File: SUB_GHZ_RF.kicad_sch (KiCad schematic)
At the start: 231 parts, among them J3 SMA4, J4 SMA1_CH-A_50R, J5 SMA2_CH-B_50R, J6 SMA3_CH-C_50R, T1 B0310J50100AHF, T2 B0310J50100AHF, T3 B0310J50100AHF, U10 BGS12WN6E6327XTSA1, U12 BGS12WN6E6327XTSA1, U14 TQP3M9036, U15 TSS-13LN+, U16 TCA9535PWR, U17 TQP3M9036, U18 BGS13SN8, U19 BGS13SN8, U20 BGS13SN8E6327XTSA1, U21 BGS13SN8E6327XTSA1, U22 TQP7M9106, U27 TPS22918DBVR, U28 BGS12P2L6, U29 BGS12P2L6, U3 CC1101RGPR, U30 BGS12P2L6, U31 BGS12P2L6, U4 CC1101RGPR, U5 CC1101RGPR, U6 SI4463-C2A-GM, U7 BGS12WN6E6327XTSA1, U8 BGS13SN8E6327XTSA1, U9 BGS13SN8E6327XTSA1, Y1 Epson X1E0000210143, Y2 Epson X1E0000210143, Y3 Epson X1E0000210143, Y4 NX2016SA

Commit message: Finished Last sheets
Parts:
- R59, R62: value 33k -> 10k
- R60, R61: value 10k -> 33k
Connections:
- net GND: no longer U6.5 (NC)
- no-connect marks 8 -> 9
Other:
- moved on the sheet: C42

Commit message: finished annotation
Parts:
- removed R44, R45: 10k, symbol Device:R
- added D15: RClamp2451ZA, Diode_SMD:Nexperia_DSN0603-2_0.6x0.3mm_P0.4mm, symbol Device:D_TVS
- added R141, R58, R59: 10k, symbol Device:R
- C60: renamed from C135; value 60u -> 68u
- D1: footprint (none) -> Diode_SMD:Nexperia_DSN0603-2_0.6x0.3mm_P0.4mm
- D2: value RF_ESD_SMA2_TBD -> RCLAMP2451ZA
- D3: value RF_ESD_SMA3_TBD -> PESD5V0Z1BDSF
- J3, J5, J6: footprint (none) -> Connector_Coaxial:SMA_Amphenol_132289_EdgeMount
- L22: value 18n -> TUNE
- R60: renamed from R62; value 10k -> 0R
- R61: value 33k -> 10k
- U14, U17: footprint TQP3M9036:SON50P200X200X95-9N -> TQP3M:SON50P200X200X95-9N
- U18, U19: value BGS13SN8 -> BGS13SN8E6327XTSA1
- U3, U4, U5: footprint CC1101RGPR:QFN50P400X400X100-21N -> CC1101:QFN50P400X400X100-21N
- Y1, Y2, Y3: footprint (none) -> Crystal:Crystal_SMD_3225-4Pin_3.2x2.5mm
- Y4: value NX2016SA -> NX2016SA-30.000MHz-EXS00A-CS06568
- renumbered C122 to C100, C123 to C101, C124 to C102, C48 to C103, C43 to C104, C44 to C105, C45 to C106, C46 to C107, C47 to C108, C89 to C109, C90 to C110, C49 to C111, C50 to C112, C87 to C113, C86 to C114, C88 to C115, C51 to C116, C52 to C117, C42 to C118, C94 to C119, C99 to C120, C93 to C121, C95 to C122, C97 to C123, C98 to C124, C96 to C125, C66 to C126, C67 to C127, C68 to C128, C70 to C129, C72 to C130, C73 to C131, C69 to C132, C71 to C134, C64 to C135, C65 to C136, C74 to C137, C112 to C138, C113 to C139, C114 to C140, C100 to C141, C101 to C142, C103 to C143, C102 to C144, C115 to C145, C116 to C146, C117 to C147, C104 to C148, C41 to C149, C78 to C42, C84 to C43, C85 to C44, C75 to C45, C76 to C46, C77 to C47, C80 to C48, C79 to C49, C81 to C50, C82 to C51, C83 to C52, C128 to C53, C127 to C54, C126 to C55, C125 to C56, C136 to C57, C138 to C58, C137 to C59, C134 to C61, C133 to C62, C132 to C63, C131 to C64, C129 to C65, C130 to C66, C139 to C67, C140 to C68, C141 to C69, C142 to C70, C143 to C71, C144 to C72, C145 to C73, C146 to C74, C147 to C75, C109 to C76, C110 to C77, C111 to C78, C58 to C79, C60 to C80, C54 to C81, C55 to C82, C63 to C83, C53 to C84, C56 to C85, C57 to C86, C59 to C87, C61 to C88, C62 to C89, C105 to C90, C106 to C91, C107 to C92, C108 to C93, C91 to C94, C92 to C95, C120 to C96, C119 to C97, C118 to C98, C121 to C99, R58 to R139, R56 to R32, R54 to R33, R55 to R34, R65 to R35, R64 to R36, R57 to R37, R47 to R38, R49 to R39, R48 to R40, R60 to R41, R59 to R42, R75 to R43, R71 to R44, R70 to R45, R67 to R46, R66 to R47, R74 to R48, R72 to R49, R73 to R50, R69 to R51, R68 to R52, R52 to R53, R50 to R54, R76 to R55, R53 to R56, R51 to R57, R63 to R62, R37 to R63, R38 to R64, R36 to R65, R34 to R66, R35 to R67, R32 to R68, R31 to R69, R46 to R70, R42 to R71, R41 to R72, R40 to R73, R39 to R74
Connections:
- net +3V3: now also R61.1; no longer FB6.1
- net +5V_SYS: now also FB6.1
- net CC1101_A_SMA1_PORT: now also D15.2 (A2)
- net GND: now also D15.1 (A1), R58.2, R59.2; no longer R61.1
- net RFX_SAW_C_SEL0: now also R58.1
- net RFX_SAW_C_SEL1: now also R59.1
- net SI4463_SDN: now also R141.2
- net VCC_SI4463: now also R141.1
- net SI4463_nIRQ renamed SI4463_IRQ_N
- no-connect marks 9 -> 11
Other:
- note added: "CHANNEL B — CC1101 + PA2 + SMA2"
- note added: "Firmware Notes CHANNEL-A SAFE DEFAULT: SEL1=0, SEL0=0, RF_SW_A=0, LNA_SD_A=1, PA_SD_A=1. TX SEQUENCE: Disable LNA → select band → select TX path → enable PA → start CC1101 transmission. TX STOP: Stop CC1101 → disable PA → wait ≥10 us → select RX path → enable LNA. GDO0/REPLAY_OUT: Never drive REPLAY_OUT while CC1101 GDO0 is configured as a push-pull output."
- note added: "Firmware note: SAFE DEFAULT: SEL1=0, SEL0=0, PA_EN_B=0. SELECT BAND BEFORE ENABLING PA. DISABLE PA BEFORE CHANGING BAND."
- note added: "PA INPUT/OUTPUT MATCHING AND 315/433/868 MHz LPF VALUES REQUIRE RF SIMULATION AND VNA TUNING BEFORE PRODUCTION"
- note added: "SHARED SUB-GHz CONTROL, SAFE STARTUP & RF RAIL FILTERING"
- note added: "SMA4 / SI4463 REV-A RF MATCHING: 868 MHz ONLY"
- note removed: ". CHANNEL B — CC1101 + PA2 + SMA2"
- note removed: "SHARED RF CONTROL"
- note removed: "SMA1 ESD DEVICE TBD AFTER PA1 POUT/VSWR IS FROZEN"
- note removed: "U7 + J3 — ANTENNA SWITCH AND SMA4"
- title: (none) -> Sub-GHz RF Transceivers, Front Ends and Band-Selectable
- moved on the sheet: R61

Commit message: finished ANCHOR_DOCK sheet
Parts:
- removed C60: 68u, symbol Device:C
- removed R52: TUNE, symbol Device:R
- added C60: 68u, symbol Device:C_Polarized
- added J17: SMA5_RESERVED_CC1200, Connector_Coaxial:SMA_Amphenol_132289_EdgeMount, symbol Connector:Conn_Coaxial
- added J18: SMA6_RESERVED_DUAL_RF, Connector_Coaxial:SMA_Amphenol_132289_EdgeMount, symbol Connector:Conn_Coaxial
- added L36: 4n7, Inductor_SMD:L_0402_1005Metric, symbol Device:L
- C100, C97: footprint (none) -> Capacitor_SMD:C_0603_1608Metric; DISTRIBUTOR_LINK (none) -> https://www.mouser.com/ProductDetail/Murata-Electronics/GRM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; MANUFACTURER (none) -> Murata; MPN (none) -> GRM188R71A225KE15D; Notes (none) -> N/A
- C101, C61, C63: footprint (none) -> Capacitor_SMD:C_0402_1005Metric; DISTRIBUTOR_LINK (none) -> https://www.mouser.com/ProductDetail/Murata-Electronics/GRM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; MANUFACTURER (none) -> Murata; MPN (none) -> GRM1555C1H102JA01D; Notes (none) -> N/A
- C102: footprint (none) -> Capacitor_SMD:C_0805_2012Metric; DISTRIBUTOR_LINK (none) -> https://www.mouser.com/ProductDetail/Murata-Electronics/GRM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; MANUFACTURER (none) -> Murata; MPN (none) -> GRM21BR71A106KE51L; Notes (none) -> Verify effective capacitance under DC bias.
- C103, C104, C105, C106, C107, C108, C112, C118, C119, C121, C126, C127, C128, C129, C130, C131, C134, C137, C147, C148, C149, C42, C46, C47, C80, C83, C84, C85, C86, C87, C88, C89, C90, C93, C94, C95, C98, C99: footprint (none) -> Capacitor_SMD:C_0402_1005Metric; DISTRIBUTOR_LINK (none) -> https://www.mouser.com/ProductDetail/Murata-Electronics/GRM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; MANUFACTURER (none) -> Murata; MPN (none) -> GRM155R71C104KA88D; Notes (none) -> N/A
- C109, C145, C91: footprint (none) -> Capacitor_SMD:C_0402_1005Metric; DISTRIBUTOR_LINK (none) -> N/A; MANUFACTURER (none) -> DNP; MPN (none) -> N/A; Notes (none) -> DNP; tuning pads retained.
- C110, C146, C92: footprint (none) -> Capacitor_SMD:C_0402_1005Metric; DISTRIBUTOR_LINK (none) -> https://www.mouser.com/ProductDetail/Murata-Electronics/GJM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; MANUFACTURER (none) -> Murata; MPN (none) -> GJM1555C1H1R2BB01D; Notes (none) -> N/A
- C111, C124, C132, C143, C45, C58, C79: footprint (none) -> Capacitor_SMD:C_0603_1608Metric; DISTRIBUTOR_LINK (none) -> https://www.mouser.com/ProductDetail/Murata-Electronics/GRM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; MANUFACTURER (none) -> Murata; MPN (none) -> GRM188R71C105KA12D; Notes (none) -> N/A
- C113, C115, C120, C122, C123, C125, C138, C139, C141, C142, C144, C53, C57, C59, C62, C76, C77: footprint (none) -> Capacitor_SMD:C_0402_1005Metric; DISTRIBUTOR_LINK (none) -> https://eu.mouser.com/en/ProductDetail/Murata-Electronics/G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; MANUFACTURER (none) -> Murata; MPN (none) -> GRM1555C1H101JA01D
- C114, C140, C78: footprint (none) -> Capacitor_SMD:C_0402_1005Metric; DISTRIBUTOR_LINK (none) -> https://www.mouser.com/ProductDetail/Murata-Electronics/GJM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; MANUFACTURER (none) -> Murata; MPN (none) -> GJM1555C1HR60BB01D; Notes (none) -> N/A
- C116, C117, C135, C136, C81, C82: footprint (none) -> Capacitor_SMD:C_0402_1005Metric; DISTRIBUTOR_LINK (none) -> https://www.mouser.com/ProductDetail/Murata-Electronics/GJM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; MANUFACTURER (none) -> Murata; MPN (none) -> GJM1555C1H150JB01D; Notes (none) -> N/A
- C43, C44: footprint (none) -> Capacitor_SMD:C_0402_1005Metric; DISTRIBUTOR_LINK (none) -> https://www.mouser.com/ProductDetail/Murata-Electronics/GJM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; MANUFACTURER (none) -> Murata; MPN (none) -> GJM1555C1H4R7BB01D; Notes (none) -> N/A
- C48: footprint (none) -> Capacitor_SMD:C_0402_1005Metric; DISTRIBUTOR_LINK (none) -> https://www.mouser.com/ProductDetail/Murata-Electronics/GJM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; MANUFACTURER (none) -> Murata; MPN (none) -> GJM1555C1H1R0BB01D; Notes (none) -> N/A
- C49: footprint (none) -> Capacitor_SMD:C_0402_1005Metric; DISTRIBUTOR_LINK (none) -> https://www.mouser.com/ProductDetail/Murata-Electronics/GJM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; MANUFACTURER (none) -> Murata; MPN (none) -> GJM1555C1H3R0BB01D; Notes (none) -> N/A
- C50: footprint (none) -> Capacitor_SMD:C_0402_1005Metric; DISTRIBUTOR_LINK (none) -> https://www.mouser.com/ProductDetail/Murata-Electronics/GJM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; MANUFACTURER (none) -> Murata; MPN (none) -> GJM1555C1H3R9BB01D; Notes (none) -> N/A
- C51: footprint (none) -> Capacitor_SMD:C_0402_1005Metric; DISTRIBUTOR_LINK (none) -> https://www.mouser.com/ProductDetail/Murata-Electronics/GJM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; MANUFACTURER (none) -> Murata; MPN (none) -> GJM1555C1H5R1BB01D; Notes (none) -> N/A
- C52: footprint (none) -> Capacitor_SMD:C_0402_1005Metric; DISTRIBUTOR_LINK (none) -> https://www.mouser.com/ProductDetail/Murata-Electronics/GJM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; MANUFACTURER (none) -> Murata; MPN (none) -> GJM1555C1H2R7BB01D; Notes (none) -> N/A
- C54: value TUNE -> 100p; footprint (none) -> Capacitor_SMD:C_0402_1005Metric; DISTRIBUTOR_LINK (none) -> https://eu.mouser.com/en/ProductDetail/Murata-Electronics/G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; MANUFACTURER (none) -> Murata; MPN (none) -> GRM1555C1H101JA01D; Notes (none) -> C0G; initial PA input match; tune on Rev-A.; TUNING_ALTERNATIVES (none) -> ALT-HB:22p; KIT:47p,68p
- C55: value TUNE -> 8p2; footprint (none) -> Capacitor_SMD:C_0402_1005Metric; DISTRIBUTOR_LINK (none) -> https://www.mouser.com/ProductDetail/Murata-Electronics/GJM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; MANUFACTURER (none) -> Murata; MPN (none) -> GJM1555C1H8R2DB01D; Notes (none) -> Initial PA input match; tuning alternatives: DNP, 5.6pF.; TUNING_ALTERNATIVES (none) -> ALT-HB:DNP; KIT:5.6p,6.8p
- C56: value TUNE -> 15p; footprint (none) -> Capacitor_SMD:C_0402_1005Metric; DISTRIBUTOR_LINK (none) -> https://www.mouser.com/ProductDetail/Murata-Electronics/GJM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; MANUFACTURER (none) -> Murata; MPN (none) -> GJM1555C1H150JB01D; Notes (none) -> Initial PA input match; tuning alternative: DNP.; TUNING_ALTERNATIVES (none) -> ALT-HB:5.6p; KIT:8.2p,12p
- C64: value 100p -> 22p; footprint (none) -> Capacitor_SMD:C_0402_1005Metric; DISTRIBUTOR_LINK (none) -> https://eu.mouser.com/en/ProductDetail/Murata-Electronics/G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; MANUFACTURER (none) -> Murata; MPN (none) -> GJM1555C1H220JB01D; Notes (none) -> N/A; TUNING_ALTERNATIVES (none) -> ALT-HB:22p; KIT:47p,100p
- C65: value TUNE -> 22p; footprint (none) -> Capacitor_SMD:C_0402_1005Metric; DISTRIBUTOR_LINK (none) -> https://eu.mouser.com/en/ProductDetail/Murata-Electronics/G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; MANUFACTURER (none) -> Murata Electronics; MPN (none) -> GJM1555C1H220JB01D; Notes (none) -> N/A; TUNING_ALTERNATIVES (none) -> ALT-HB:12p; KIT:15p,18p
- C66: value TUNE -> 6p8; footprint (none) -> Capacitor_SMD:C_0402_1005Metric; DISTRIBUTOR_LINK (none) -> https://eu.mouser.com/en/ProductDetail/Murata-Electronics/G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; MANUFACTURER (none) -> Murata Electronics; MPN (none) -> GJM1555C1H6R8CB01D; Notes (none) -> Rev-A initial fitted value; finalize with L36 by VNA and ha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; TUNING_ALTERNATIVES (none) -> ALT-HB:3.9p; KIT:4.7p,5.6p
- C67, C75: value TUNE -> 4p7; footprint (none) -> Capacitor_SMD:C_0402_1005Metric; DISTRIBUTOR_LINK (none) -> https://www.mouser.com/en/ProductDetail/Murata-Electronics/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; MANUFACTURER (none) -> Murata; MPN (none) -> GJM1555C1H4R7BB01D; Notes (none) -> Rev-A initial fitted value; finalize by VNA/harmonic testin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; TUNING_ALTERNATIVES (none) -> 4.3p,5.1p
- C68: value TUNE -> 15p; footprint (none) -> Capacitor_SMD:C_0402_1005Metric; DISTRIBUTOR_LINK (none) -> https://www.mouser.com/en/ProductDetail/Murata-Electronics/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; MANUFACTURER (none) -> Murata; MPN (none) -> GJM1555C1H150JB01D; Notes (none) -> Rev-A initial fitted value; finalize by VNA/harmonic testin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; TUNING_ALTERNATIVES (none) -> 13p,16p
- C69: value TUNE -> 13p; footprint (none) -> Capacitor_SMD:C_0402_1005Metric; DISTRIBUTOR_LINK (none) -> https://www.mouser.com/en/ProductDetail/Murata-Electronics/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; MANUFACTURER (none) -> Murata; MPN (none) -> GJM1555C1H130JB01D; Notes (none) -> Rev-A initial fitted value; finalize by VNA/harmonic testin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; TUNING_ALTERNATIVES (none) -> 12p,15p
- C70: value TUNE -> 3p3; footprint (none) -> Capacitor_SMD:C_0402_1005Metric; DISTRIBUTOR_LINK (none) -> https://www.mouser.com/en/ProductDetail/Murata-Electronics/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; MANUFACTURER (none) -> Murata; MPN (none) -> GJM1555C1H3R3BB01D; Notes (none) -> Rev-A initial fitted value; finalize by VNA/harmonic testin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; TUNING_ALTERNATIVES (none) -> 3.0p,3.6p
- C71: value TUNE -> 11p; footprint (none) -> Capacitor_SMD:C_0402_1005Metric; DISTRIBUTOR_LINK (none) -> https://www.mouser.com/en/ProductDetail/Murata-Electronics/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; MANUFACTURER (none) -> Murata; MPN (none) -> GJM1555C1H110JB01D; Notes (none) -> Rev-A initial fitted value; finalize by VNA/harmonic testin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; TUNING_ALTERNATIVES (none) -> 10p,12p
- C72: value TUNE -> 9p1; footprint (none) -> Capacitor_SMD:C_0402_1005Metric; DISTRIBUTOR_LINK (none) -> https://www.mouser.com/en/ProductDetail/Murata-Electronics/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; MANUFACTURER (none) -> Murata; MPN (none) -> GJM1555C1H9R1DB01D; Notes (none) -> Rev-A initial fitted value; finalize by VNA/harmonic testin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; TUNING_ALTERNATIVES (none) -> 8.2p,10p
- C73: value TUNE -> 1p8; footprint (none) -> Capacitor_SMD:C_0402_1005Metric; DISTRIBUTOR_LINK (none) -> https://www.mouser.com/en/ProductDetail/Murata-Electronics/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; MANUFACTURER (none) -> Murata; MPN (none) -> GJM1555C1H1R8BB01D; Notes (none) -> Rev-A initial fitted value; finalize by VNA/harmonic testin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; TUNING_ALTERNATIVES (none) -> 1.5p,2.0p
- C74: value TUNE -> 5p6; footprint (none) -> Capacitor_SMD:C_0402_1005Metric; DISTRIBUTOR_LINK (none) -> https://www.mouser.com/en/ProductDetail/Murata-Electronics/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; MANUFACTURER (none) -> Murata; MPN (none) -> GJM1555C1H5R6BB01D; Notes (none) -> Rev-A initial fitted value; finalize by VNA/harmonic testin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; TUNING_ALTERNATIVES (none) -> 5.1p,6.2p
- C96: footprint (none) -> Capacitor_SMD:C_0402_1005Metric; DISTRIBUTOR_LINK (none) -> https://www.mouser.com/ProductDetail/Murata-Electronics/GJM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; MANUFACTURER (none) -> Murata; MPN (none) -> GJM1555C1H1R5BB01D; Notes (none) -> N/A
- D1: value PESD5V0Z1BDSF -> PESD5V0F1BRSF; DISTRIBUTOR_LINK (none) -> https://www.digikey.com/en/products/detail/nexperia-usa-inc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; MANUFACTURER (none) -> Nexperia; MPN (none) -> PESD5V0F1BRSFYL; Notes (none) -> PCBWay: source exact DSN0603-2 part; no package change.
- D15: footprint Diode_SMD:Nexperia_DSN0603-2_0.6x0.3mm_P0.4mm -> (none); DISTRIBUTOR_LINK (none) -> https://www.mouser.com/ProductDetail/Semtech/RCLAMP2451ZATF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; MANUFACTURER (none) -> Semtech; MPN (none) -> RCLAMP2451ZATFT; Notes (none) -> Custom SLP0603P2X3F footprint required.
- D2: DISTRIBUTOR_LINK (none) -> https://www.mouser.com/ProductDetail/Semtech/RCLAMP2451ZATF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; MANUFACTURER (none) -> Semtech; MPN (none) -> RCLAMP2451ZATFT; Notes (none) -> Custom SLP0603P2X3F footprint required.
- D3: value PESD5V0Z1BDSF -> PESD5V0F1BRSF; footprint (none) -> Diode_SMD:Nexperia_DSN0603-2_0.6x0.3mm_P0.4mm; DISTRIBUTOR_LINK (none) -> https://www.digikey.com/en/products/detail/nexperia-usa-inc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; MANUFACTURER (none) -> Nexperia; MPN (none) -> PESD5V0F1BRSFYL; Notes (none) -> PCBWay: source exact DSN0603-2 part; no package change.
- FB1, FB2, FB3, FB4, FB5, FB6: footprint (none) -> Inductor_SMD:L_0402_1005Metric; DISTRIBUTOR_LINK (none) -> https://www.mouser.com/ProductDetail/Murata-Electronics/BLM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; MANUFACTURER (none) -> Murata; MPN (none) -> BLM15AG601SN1D; Notes (none) -> 300 mA rated bead; adequate for the CC1101, Si4463 and LNA 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
- FL10, FL4, FL7: DISTRIBUTOR_LINK (none) -> https://www.mouser.com/ProductDetail/RF360/B39871B3725U410?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; MANUFACTURER EPCOS -> TDK/EPCOS; MPN (none) -> B39871B3725U410; Notes (none) -> N/A
- FL11, FL3, FL8: DISTRIBUTOR_LINK (none) -> https://www.mouser.com/ProductDetail/RF360/B39431B3710U410?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; MANUFACTURER EPCOS -> TDK/EPCOS; MPN (none) -> B39431B3710U410; Notes (none) -> N/A
- FL12, FL2, FL9: DISTRIBUTOR_LINK (none) -> https://www.mouser.com/ProductDetail/RF360/B39321B3722U410?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; MANUFACTURER EPCOS -> TDK/EPCOS; MPN (none) -> B39321B3722U410; Notes (none) -> N/A
- J3, J4, J5, J6: DISTRIBUTOR_LINK (none) -> https://www.mouser.com/ProductDetail/Amphenol-RF/132289?qs=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; MANUFACTURER (none) -> Amphenol RF; MPN (none) -> 132289; Notes (none) -> Manual/post-reflow SMA assembly.
- L10, L9: footprint (none) -> Inductor_SMD:L_0402_1005Metric; DISTRIBUTOR_LINK (none) -> https://eu.mouser.com/en/ProductDetail/Murata-Electronics/L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; MANUFACTURER (none) -> Murata; MPN (none) -> LQG15WZ11NH02D
- L11: footprint (none) -> Inductor_SMD:L_0402_1005Metric; DISTRIBUTOR_LINK (none) -> https://eu.mouser.com/en/ProductDetail/Murata-Electronics/L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; MANUFACTURER (none) -> Murata; MPN (none) -> LQG15HH9N1J02D
- L12, L16, L18: footprint (none) -> Inductor_SMD:L_0402_1005Metric; DISTRIBUTOR_LINK (none) -> https://www.mouser.com/ProductDetail/Murata-Electronics/LQG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; MANUFACTURER (none) -> Murata; MPN (none) -> LQG15HS3N3S02D; Notes (none) -> N/A
- L13, L17, L19: footprint (none) -> Inductor_SMD:L_0402_1005Metric; DISTRIBUTOR_LINK (none) -> https://eu.mouser.com/en/ProductDetail/Murata-Electronics/L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; MANUFACTURER (none) -> Murata; MPN (none) -> LQG15HH6N8J02D; Notes (none) -> Exact Rev-A fitted RF inductor; no substitution without RF 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
- L14, L15, L23: footprint (none) -> Inductor_SMD:L_0402_1005Metric; DISTRIBUTOR_LINK (none) -> https://www.mouser.com/ProductDetail/Murata-Electronics/LQG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; MANUFACTURER (none) -> Murata; MPN (none) -> LQG15HS68NJ02D; Notes (none) -> N/A
- L20: footprint (none) -> Inductor_SMD:L_0402_1005Metric; DISTRIBUTOR_LINK (none) -> https://www.mouser.com/ProductDetail/Murata-Electronics/LQG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; MANUFACTURER (none) -> Murata; MPN (none) -> LQG15HS5N1S02D; Notes (none) -> N/A
- L21: DISTRIBUTOR_LINK (none) -> https://www.mouser.com/ProductDetail/Murata-Electronics/LQH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; MANUFACTURER (none) -> Murata; MPN (none) -> LQH44PN150MPRL; Notes (none) -> 1.1 A temperature-rise / 1.3 A saturation rating; adequate 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
- L22: value TUNE -> 18n; footprint (none) -> Inductor_SMD:L_1008_2520Metric; DISTRIBUTOR_LINK (none) -> https://www.mouser.com/ProductDetail/ABRACON/AISC-1008HQ-18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; MANUFACTURER (none) -> Abracon; MPN (none) -> AISC-1008HQ-18NJ-T; Notes (none) -> PA bias choke. Coilcraft 1008HQ-18NXJLC is Qorvo-reference 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
- L24: value TUNE -> 33n; footprint (none) -> Inductor_SMD:L_0603_1608Metric; DISTRIBUTOR_LINK (none) -> https://www.mouser.com/en/ProductDetail/Murata-Electronics/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; MANUFACTURER (none) -> Murata; MPN (none) -> LQW18AN33NJ00D; Notes (none) -> Rev-A initial fitted value; finalize by VNA/harmonic testin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; TUNING_ALTERNATIVES (none) -> 30n,36n
- L25: value TUNE -> 39n; footprint (none) -> Inductor_SMD:L_0603_1608Metric; DISTRIBUTOR_LINK (none) -> https://www.mouser.com/en/ProductDetail/Murata-Electronics/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; MANUFACTURER (none) -> Murata; MPN (none) -> LQW18AN39NJ00D; Notes (none) -> Rev-A initial fitted value; finalize by VNA/harmonic testin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; TUNING_ALTERNATIVES (none) -> 36n,43n
- L26, L30: value TUNE -> 12n; footprint (none) -> Inductor_SMD:L_0603_1608Metric; DISTRIBUTOR_LINK (none) -> https://www.mouser.com/en/ProductDetail/Murata-Electronics/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; MANUFACTURER (none) -> Murata; MPN (none) -> LQW18AN12NJ00D; Notes (none) -> Rev-A initial fitted value; finalize by VNA/harmonic testin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; TUNING_ALTERNATIVES (none) -> 11n,13n
- L27: value TUNE -> 24n; footprint (none) -> Inductor_SMD:L_0603_1608Metric; DISTRIBUTOR_LINK (none) -> https://www.mouser.com/en/ProductDetail/Murata-Electronics/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; MANUFACTURER (none) -> Murata; MPN (none) -> LQW18AN24NJ00D; Notes (none) -> Rev-A initial fitted value; finalize by VNA/harmonic testin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; TUNING_ALTERNATIVES (none) -> 22n,27n
- L28: value TUNE -> 27n; footprint (none) -> Inductor_SMD:L_0603_1608Metric; DISTRIBUTOR_LINK (none) -> https://www.mouser.com/en/ProductDetail/Murata-Electronics/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; MANUFACTURER (none) -> Murata; MPN (none) -> LQW18AN27NJ00D; Notes (none) -> Rev-A initial fitted value; finalize by VNA/harmonic testin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; TUNING_ALTERNATIVES (none) -> 24n,30n
- L29: value TUNE -> 9n1; footprint (none) -> Inductor_SMD:L_0603_1608Metric; DISTRIBUTOR_LINK (none) -> https://www.mouser.com/en/ProductDetail/Murata-Electronics/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; MANUFACTURER (none) -> Murata; MPN (none) -> LQW18AN9N1D00D; Notes (none) -> Rev-A initial fitted value; finalize by VNA/harmonic testin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; TUNING_ALTERNATIVES (none) -> 8.2n,10n
- L31: value TUNE -> 13n; footprint (none) -> Inductor_SMD:L_0603_1608Metric; DISTRIBUTOR_LINK (none) -> https://www.mouser.com/en/ProductDetail/Murata-Electronics/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; MANUFACTURER (none) -> Murata; MPN (none) -> LQW18AN13NJ00D; Notes (none) -> Rev-A initial fitted value; finalize by VNA/harmonic testin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; TUNING_ALTERNATIVES (none) -> 12n,15n
- L32: value TUNE -> 3n9; footprint (none) -> Inductor_SMD:L_0603_1608Metric; DISTRIBUTOR_LINK (none) -> https://www.mouser.com/en/ProductDetail/Murata-Electronics/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; MANUFACTURER (none) -> Murata; MPN (none) -> LQW18AN3N9C00D; Notes (none) -> Rev-A initial fitted value; finalize by VNA/harmonic testin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; TUNING_ALTERNATIVES (none) -> 3.6n,4.3n
- L5: footprint (none) -> Inductor_SMD:L_0402_1005Metric; DISTRIBUTOR_LINK (none) -> https://eu.mouser.com/en/ProductDetail/Murata-Electronics/L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; MANUFACTURER (none) -> Murata; MPN (none) -> LQG15WZ20NH02D
- L6: footprint (none) -> Inductor_SMD:L_0402_1005Metric; DISTRIBUTOR_LINK (none) -> https://eu.mouser.com/en/ProductDetail/Murata-Electronics/L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; MANUFACTURER (none) -> Murata; MPN (none) -> LQG15WZ24NH02D
- L7: footprint (none) -> Inductor_SMD:L_0402_1005Metric; DISTRIBUTOR_LINK (none) -> https://www.mouser.com/ProductDetail/Murata-Electronics/LQG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; MANUFACTURER (none) -> Murata; MPN (none) -> LQG15HS15NJ02D; Notes (none) -> N/A
- L8: footprint (none) -> Inductor_SMD:L_0402_1005Metric; DISTRIBUTOR_LINK (none) -> https://www.mouser.com/ProductDetail/Murata-Electronics/LQG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; MANUFACTURER (none) -> Murata; MPN (none) -> LQG15HSR12J02D; Notes (none) -> N/A
- R139, R37, R45, R49, R50, R60, R62: footprint (none) -> Resistor_SMD:R_0603_1608Metric; DISTRIBUTOR_LINK (none) -> https://www.mouser.com/ProductDetail/YAGEO/RC0603JR-070RL?q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; MANUFACTURER (none) -> Yageo; MPN (none) -> RC0603JR-070RL; Notes (none) -> N/A
- R141, R32, R33, R35, R38, R42, R53, R55, R56, R58, R59, R61, R63, R64, R65, R66, R67, R68, R69, R70, R71, R72, R73, R74: footprint (none) -> Resistor_SMD:R_0603_1608Metric; DISTRIBUTOR_LINK (none) -> https://www.mouser.com/ProductDetail/YAGEO/RC0603FR-0710KL?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; MANUFACTURER (none) -> Yageo; MPN (none) -> RC0603FR-0710KL; Notes (none) -> N/A
- R34, R39: footprint (none) -> Resistor_SMD:R_0603_1608Metric; DISTRIBUTOR_LINK (none) -> https://www.mouser.com/ProductDetail/Yageo/RC0603FR-071KL?q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; MANUFACTURER (none) -> Yageo; MPN (none) -> RC0603FR-071KL; Notes (none) -> N/A
- R36: footprint (none) -> Resistor_SMD:R_0603_1608Metric; DISTRIBUTOR_LINK (none) -> https://www.mouser.com/ProductDetail/YAGEO/RC0603FR-071K5L?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; MANUFACTURER (none) -> Yageo; MPN (none) -> RC0603FR-071K5L; Notes (none) -> N/A
- R40, R54, R57: footprint (none) -> Resistor_SMD:R_0603_1608Metric; DISTRIBUTOR_LINK (none) -> https://www.mouser.com/ProductDetail/YAGEO/RC0603FR-0756KL?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; MANUFACTURER (none) -> Yageo; MPN (none) -> RC0603FR-0756KL; Notes (none) -> N/A
- R41: footprint (none) -> Resistor_SMD:R_0603_1608Metric; DISTRIBUTOR_LINK (none) -> https://www.mouser.com/ProductDetail/YAGEO/RC0603FR-0733KL?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; MANUFACTURER (none) -> Yageo; MPN (none) -> RC0603FR-0733KL; Notes (none) -> N/A
- R43: footprint (none) -> Resistor_SMD:R_0603_1608Metric; DISTRIBUTOR_LINK (none) -> https://www.mouser.com/ProductDetail/YAGEO/RC0603FR-07100KL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; MANUFACTURER (none) -> Yageo; MPN (none) -> RC0603FR-07100KL; Notes (none) -> N/A
- R44, R48: footprint (none) -> Resistor_SMD:R_0603_1608Metric; DISTRIBUTOR_LINK (none) -> https://www.mouser.com/ProductDetail/YAGEO/RC0603FR-07280RL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; MANUFACTURER (none) -> Yageo; MPN (none) -> RC0603FR-07280RL; Notes (none) -> N/A
- R46: value TUNE -> 51R; footprint (none) -> Resistor_SMD:R_0402_1005Metric; DISTRIBUTOR_LINK (none) -> https://eu.mouser.com/en/ProductDetail/YAGEO/RC0402FR-0751R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; MANUFACTURER (none) -> Yageo; MPN (none) -> RC0402FR-0751RL; Notes (none) -> Initial PA input match; tune on Rev-A.
- R47: value TUNE -> 4R3; footprint (none) -> Resistor_SMD:R_0402_1005Metric; DISTRIBUTOR_LINK (none) -> https://www.mouser.com/ProductDetail/YAGEO/RC0402FR-074R3L?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; MANUFACTURER (none) -> Yageo; MPN (none) -> RC0402FR-074R3L; Notes (none) -> Initial PA input damping/match; verify during Rev-A RF tuni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
- R51: footprint (none) -> Resistor_SMD:R_0805_2012Metric; DISTRIBUTOR_LINK (none) -> https://www.mouser.com/ProductDetail/Panasonic/ERJ-6GEY0R00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; MANUFACTURER (none) -> Panasonic; MPN (none) -> ERJ-6GEY0R00V; Notes (none) -> 2 A rated jumper; suitable for PA supply.
- T1, T2, T3: DISTRIBUTOR_LINK (none) -> https://www.mouser.com/ProductDetail/TTM-Technologies/B0310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; MANUFACTURER Anaren -> TTM Technologies; MPN (none) -> B0310J50100AHF; Notes (none) -> N/A
- U10, U12, U7: DISTRIBUTOR_LINK (none) -> https://www.mouser.com/ProductDetail/Infineon-Technologies/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; MANUFACTURER (none) -> Infineon; MPN (none) -> BGS12WN6E6327XTSA1; Notes (none) -> Assembly: verify RF-switch pin-1 orientation.
- U14, U17: DISTRIBUTOR_LINK (none) -> https://www.mouser.com/ProductDetail/Qorvo/TQP3M9036?qs=73o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; MPN (none) -> TQP3M9036; Notes (none) -> Assembly: follow RF land pattern and EP grounding.
- U15: DISTRIBUTOR_LINK (none) -> https://www.mouser.com/ProductDetail/Mini-Circuits/TSS-13LN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; MANUFACTURER (none) -> Mini-Circuits; MPN (none) -> TSS-13LN+; Notes (none) -> PCBWay: inspect exposed-pad voiding/X-ray.
- U16: DISTRIBUTOR_LINK (none) -> https://www.mouser.com/ProductDetail/Texas-Instruments/TCA9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; MANUFACTURER (none) -> Texas Instruments; MPN (none) -> TCA9535PWR; Notes (none) -> N/A
- U18, U19, U20, U21, U8, U9: DISTRIBUTOR_LINK (none) -> https://www.mouser.com/ProductDetail/Infineon-Technologies/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; MANUFACTURER (none) -> Infineon; MPN (none) -> BGS13SN8E6327XTSA1; Notes (none) -> Check pin-1 and package orientation.
- U22: DISTRIBUTOR_LINK (none) -> https://www.mouser.com/ProductDetail/Qorvo/TQP7M9106?qs=ZyJ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; MPN (none) -> TQP7M9106; Notes (none) -> Assembly: EP vias, thermal review, X-ray; RF tune.
- U27: DISTRIBUTOR_LINK (none) -> https://www.mouser.com/ProductDetail/Texas-Instruments/TPS2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; MANUFACTURER (none) -> Texas Instruments; MPN (none) -> TPS22918DBVR; Notes (none) -> N/A
- U28, U29, U30, U31: DISTRIBUTOR_LINK (none) -> https://www.mouser.com/ProductDetail/Infineon-Technologies/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; MANUFACTURER (none) -> Infineon; MPN (none) -> BGS12P2L6E6327XTSA1; Notes (none) -> N/A
- U3, U4, U5: DISTRIBUTOR_LINK (none) -> https://www.mouser.com/ProductDetail/Texas-Instruments/CC11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; MPN (none) -> CC1101RGPR; Notes (none) -> Assembly: QFN exposed pad grounded; X-ray.
- U6: DISTRIBUTOR_LINK (none) -> https://www.mouser.com/ProductDetail/Silicon-Labs/SI4463-C2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; MANUFACTURER (none) -> Silicon Labs; MPN (none) -> SI4463-C2A-GMR; Notes (none) -> Assembly: exposed pad grounded; X-ray.
- Y1, Y2, Y3: value Epson X1E0000210143 -> ABM8-26.000MHz-10-B-1-U-T; DISTRIBUTOR_LINK (none) -> https://eu.mouser.com/en/ProductDetail/ABRACON/ABM8-26.000M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; MANUFACTURER (none) -> Abracon; MPN (none) -> ABM8-26.000MHz-10-B-1-U-T; Notes (none) -> Ground crystal case pads 2/4.
- Y4: value NX2016SA-30.000MHz-EXS00A-CS06568 -> ABM11W-30.0000MHZ-8-D1X-T3; DISTRIBUTOR_LINK (none) -> https://eu.mouser.com/en/ProductDetail/ABRACON/ABM11W-30.00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; MANUFACTURER (none) -> Abracon; MPN (none) -> ABM11W-30.0000MHZ-8-D1X-T3
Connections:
- net +5V_SYS: now also C60.1
- net CC1101_B_PA2_OUT_MATCH_N1: now also L36.2
- net CC1101_B_PA2_RF_OUT_BIASED: now also L36.1
- net GND: now also C60.2, J17.2 (Ext), J18.2 (Ext)
- no-connect marks 11 -> 13
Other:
- note added: "PA matching alternatives are tuning-only. Change values as a complete measured set; do not mix configurations independently."
- note added: "REV-A INITIAL VALUES SHOWN. ALTERNATIVES ARE VNA TUNING-KIT PARTS; DO NOT MIX VALUES WITHOUT MEASUREMENT. VERIFY HARMONICS AT OPERATING POWER."
- note removed: "PA INPUT/OUTPUT MATCHING AND 315/433/868 MHz LPF VALUES REQUIRE RF SIMULATION AND VNA TUNING BEFORE PRODUCTION"
- moved on the sheet: L5

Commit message: the schematic is finished
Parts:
- C113, C115, C120, C122, C123, C125, C138, C139, C141, C142, C144, C53, C57, C59, C62, C76, C77, L10, L11, L5, L6, L9, Y4: Notes (none) -> N/A
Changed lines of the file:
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@@
 			)
 		)
-		(property "Notes" ""
+		(property "Notes" "N/A"
 			(at 46.99 417.83 90)
 			(hide yes)
@@
 			)
 		)
-		(property "Notes" ""
+		(property "Notes" "N/A"
 			(at 304.8 101.6 0)
 			(hide yes)
@@
 			)
 		)
-		(property "Notes" ""
+		(property "Notes" "N/A"
 			(at 245.11 138.43 90)
 			(hide yes)
@@
 			)
 		)
-		(property "Notes" ""
+		(property "Notes" "N/A"
 			(at 205.74 525.78 90)
 			(hide yes)
@@
 			)
 		)
-		(property "Notes" ""
+		(property "Notes" "N/A"
 			(at 46.99 430.53 90)
 			(hide yes)
@@
 			)
 		)
-		(property "Notes" ""
+		(property "Notes" "N/A"
 			(at 518.16 391.16 90)
 			(hide yes)
@@
 			)
 		)
-		(property "Notes" ""
+		(property "Notes" "N/A"
 			(at 577.85 378.46 90)
 			(hide yes)
@@
 			)
 		)
-		(property "Notes" ""
+		(property "Notes" "N/A"
 			(at 163.83 504.19 90)
 			(hide yes)
@@
 			)
 		)
-		(property "Notes" ""
+		(property "Notes" "N/A"
 			(at 124.46 538.48 90)
 			(hide yes)
@@
 			)
 		)
-		(property "Notes" ""
+		(property "Notes" "N/A"
 			(at 363.22 181.61 90)
 			(hide yes)
@@
 			)
 		)
-		(property "Notes" ""
+		(property "Notes" "N/A"
 			(at 175.26 97.79 90)
 			(hide yes)
@@
 			)
 		)
-		(property "Notes" ""
+		(property "Notes" "N/A"
 			(at 478.79 73.66 90)
 			(hide yes)
@@
 			)
 		)
-		(property "Notes" ""
+		(property "Notes" "N/A"
 			(at 264.16 100.33 0)
 			(hide yes)
@@
 			)
 		)
-		(property "Notes" ""
+		(property "Notes" "N/A"
 			(at 240.03 439.42 90)
 			(hide yes)
@@
 			)
 		)
-		(property "Notes" ""
+		(property "Notes" "N/A"
 			(at 355.6 443.23 90)
 			(hide yes)
@@
 			)
 		)
-		(property "Notes" ""
+		(property "Notes" "N/A"
 			(at 73.66 118.11 90)
 			(hide yes)
@@
 			)
 		)
-		(property "Notes" ""
+		(property "Notes" "N/A"
 			(at 363.22 176.53 90)
 			(hide yes)
@@
 			)
 		)
-		(property "Notes" ""
+		(property "Notes" "N/A"
 			(at 355.6 448.31 90)
 			(hide yes)
@@
 			)
 		)
-		(property "Notes" ""
+		(property "Notes" "N/A"
 			(at 568.96 356.87 90)
 			(hide yes)
@@
 			)
 		)
-		(property "Notes" ""
+		(property "Notes" "N/A"
 			(at 281.94 138.43 90)
 			(hide yes)
@@
 			)
 		)
-		(property "Notes" ""
+		(property "Notes" "N/A"
 			(at 516.89 59.69 90)
 			(hide yes)
@@
 			)
 		)
-		(property "Notes" ""
+		(property "Notes" "N/A"
 			(at 401.32 76.2 90)
 			(hide yes)
@@
 			)
 		)
-		(property "Notes" ""
+		(property "Notes" "N/A"
 			(at 353.06 95.25 90)
 			(hide yes)

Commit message: finished schematic phase
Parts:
- C60: footprint (none) -> FOBtool_Custom:CP_Panasonic_EEF-LR_7.3x4.3mm_3Terminal
- D15, D2: footprint (none) -> FOBtool_Custom:D_Semtech_RCLAMP2451ZA_DFN0603_2
- L21: footprint (none) -> FOBtool_Custom:L_Murata_LQH44PN_4.0x4.0mm
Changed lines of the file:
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@@
 			)
 		)
-		(property "Footprint" ""
+		(property "Footprint" "FOBtool_Custom:L_Murata_LQH44PN_4.0x4.0mm"
 			(at 276.86 246.38 0)
 			(hide yes)
@@
 			)
 		)
-		(property "Footprint" ""
+		(property "Footprint" "FOBtool_Custom:D_Semtech_RCLAMP2451ZA_DFN0603_2"
 			(at 741.68 48.26 0)
 			(hide yes)
@@
 			)
 		)
-		(property "Footprint" ""
+		(property "Footprint" "FOBtool_Custom:CP_Panasonic_EEF-LR_7.3x4.3mm_3Terminal"
 			(at 520.7 29.5148 0)
 			(hide yes)
@@
 			)
 		)
-		(property "Footprint" ""
+		(property "Footprint" "FOBtool_Custom:D_Semtech_RCLAMP2451ZA_DFN0603_2"
 			(at 254 444.5 0)
 			(hide yes)

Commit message: adding 3d models
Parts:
- T1, T2, T3: MANUFACTURER TTM Technologies -> Anaren
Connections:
- no-connect marks 13 -> 19
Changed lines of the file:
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@@
 	)
 	(no_connect
+		(at 397.51 185.42)
+	)
+	(no_connect
 		(at 693.42 391.16)
 	)
@@
 	)
 	(no_connect
+		(at 373.38 452.12)
+	)
+	(no_connect
+		(at 434.34 452.12)
+	)
+	(no_connect
+		(at 93.98 377.19)
+	)
+	(no_connect
 		(at 226.06 115.57)
 	)
@@
 	)
 	(no_connect
+		(at 33.02 377.19)
+	)
+	(no_connect
 		(at 693.42 393.7)
 	)
@@
 		(at 657.86 358.14)
 	)
+	(no_connect
+		(at 458.47 185.42)
+	)
 	(wire
 		(pts
@@
 	(wire
 		(pts
-			(xy 93.98 373.38) (xy 95.25 373.38)
+			(xy 93.98 373.38) (xy 97.79 373.38)
 		)
 		(stroke
@@
 	(wire
 		(pts
-			(xy 95.25 373.38) (xy 95.25 377.19)
+			(xy 97.79 373.38) (xy 97.79 377.19)
 		)
 		(stroke
@@
 	(symbol
 		(lib_id "power:GND")
-		(at 95.25 377.19 0)
+		(at 97.79 377.19 0)
 		(unit 1)
 		(body_style 1)
@@
 		(fields_autoplaced yes)
 		(property "Reference" "#PWR0104"
-			(at 95.25 383.54 0)
+			(at 97.79 383.54 0)
 			(hide yes)
 			(show_name no)
@@
 		)
 		(property "Value" "GND"
-			(at 95.25 382.27 0)
+			(at 97.79 382.27 0)
 			(show_name no)
 			(do_not_autoplace no)
@@
 		)
 		(property "Footprint" ""
-			(at 95.25 377.19 0)
+			(at 97.79 377.19 0)
 			(hide yes)
 			(show_name no)
@@
 		)
 		(property "Datasheet" ""
-			(at 95.25 377.19 0)
+			(at 97.79 377.19 0)
 			(hide yes)
 			(show_name no)
@@
 		)
 		(property "Description" "Power symbol creates a global label with name \"GND\" , ground"
-			(at 95.25 377.19 0)
+			(at 97.79 377.19 0)
 			(hide yes)
 			(show_name no)
@@
 			)
 		)
-		(property "MANUFACTURER" "TTM Technologies"
+		(property "MANUFACTURER" "Anaren"
 			(at 403.86 445.77 0)
 			(hide yes)
@@
 		(pin "3"
 		)
+		(pin "6"
+		)
+		(pin "5"
+		)
 		(instances
 			(project "FOBtool_HW"
@@
 		(dnp no)
 		(property "Reference" "T2"
-			(at 452.12 185.928 0)
+			(at 452.628 188.976 0)
 			(show_name no)
 			(do_not_autoplace no)
@@
 			)
 		)
-		(property "MANUFACTURER" "TTM Technologies"
+		(property "MANUFACTURER" "Anaren"
 			(at 427.99 179.07 0)
 			(hide yes)
@@
 		(pin "3"
 		)
+		(pin "6"
+		)
+		(pin "5"
+		)
 		(instances
 			(project "FOBtool_HW"
@@
 			)
 		)
-		(property "MANUFACTURER" "TTM Technologies"
+		(property "MANUFACTURER" "Anaren"
 			(at 63.5 370.84 0)
 			(hide yes)
@@
 		(pin "3"
 		)
+		(pin "6"
+		)
+		(pin "5"
+		)
 		(instances

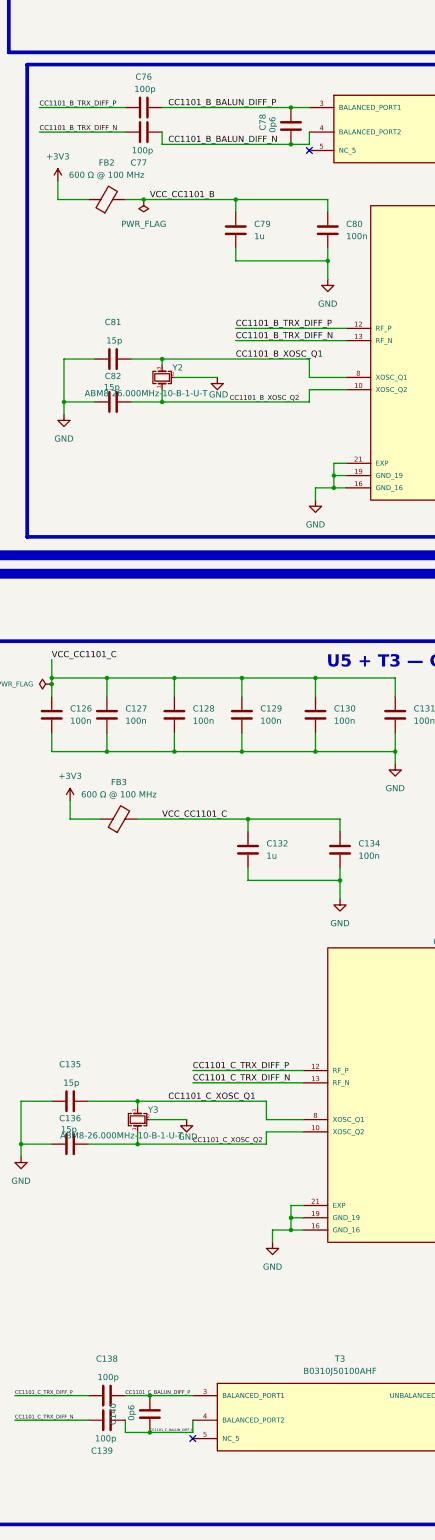
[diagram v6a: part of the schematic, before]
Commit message: changiong bootsel buttom in rp
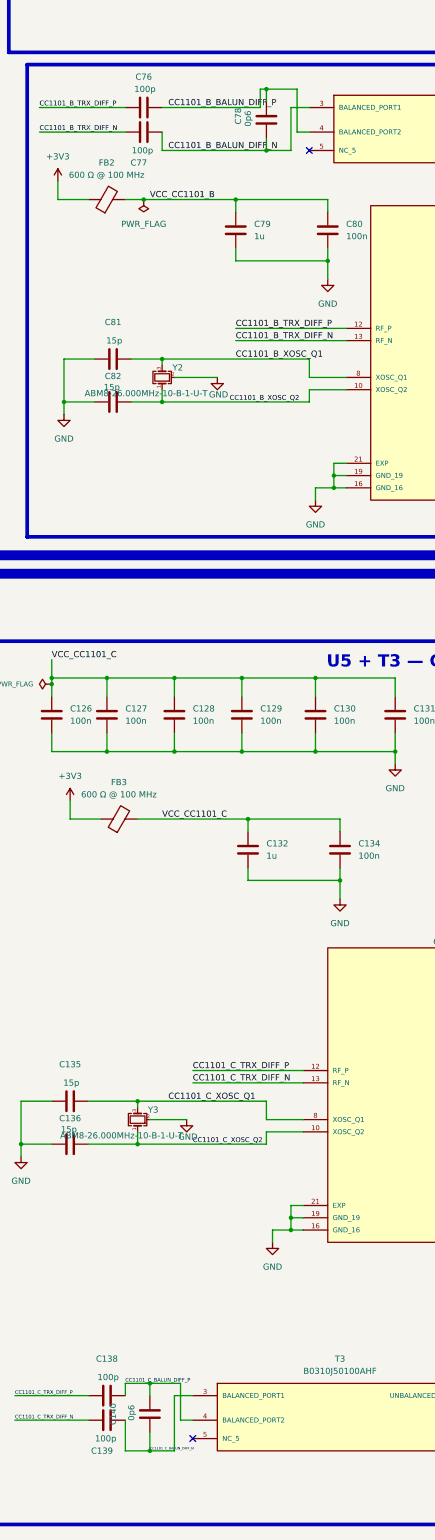
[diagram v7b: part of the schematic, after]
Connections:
- net CC1101_B_BALUN_DIFF_N: now also T2.3 (BALANCED_PORT1); no longer T2.4 (BALANCED_PORT2)
- net CC1101_B_BALUN_DIFF_P: now also T2.4 (BALANCED_PORT2); no longer T2.3 (BALANCED_PORT1)
- net CC1101_C_BALUN_DIFF_N: now also T3.3 (BALANCED_PORT1); no longer T3.4 (BALANCED_PORT2)
- net CC1101_C_BALUN_DIFF_P: now also T3.4 (BALANCED_PORT2); no longer T3.3 (BALANCED_PORT1)
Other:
- moved on the sheet: C78
